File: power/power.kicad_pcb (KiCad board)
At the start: 2 copper layers, 100 x 100 mm, 25 parts, among them K1 RELAY_SPST, K2 RELAY_SPST, K3 RELAY_SPST, P1 CONTROL, P2 MAINS_INLET, P3 LOAD_OUTLET, Q1 BC817-40, Q2 BC817-40, Q3 BC817-40, U1 VTX214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

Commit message: Power: onboard fuses, better attempt at first pcb
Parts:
- added U4: TIC206M, Transistors_TO-220:TO-220_Neutral123_Vertical_LargePads, F.Cu at (122.0, 70.0)
- F1: footprint power:fuseholder -> power:5x20_clip
- F2: footprint power:fuseholder -> power:BS1362_clip
- K1: value RELAY_SPST -> MASTER_LIVE
- K2: value RELAY_SPST -> MASTER_NEUTRAL
- K3: value RELAY_SPST -> PREHEAT
- moved C4 216.9 mm to (124.0, 63.0), turned to 180 degrees
- moved R2 195.1 mm to (96.9, 230.8)
- moved R6 195.1 mm to (101.4, 230.8)
- moved C1 176.2 mm to (48.2, 238.5)
- moved C3 176.2 mm to (67.0, 236.8)
- moved Q1 176.2 mm to (86.7, 255.6)
- moved Q2 176.2 mm to (47.3, 232.0)
- moved R1 176.2 mm to (66.7, 230.4)
- moved R3 176.2 mm to (71.2, 230.4)
- moved U5 176.2 mm to (59.6, 235.0)
- moved Q3 176.2 mm to (86.7, 263.7)
- moved R4 172.7 mm to (122.0, 88.0), turned to 270 degrees
- moved C2 165.1 mm to (61.0, 216.0)
- moved P1 164.6 mm to (115.0, 273.0)
- moved R5 134.7 mm to (118.0, 63.0), turned to 180 degrees
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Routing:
- net MAINS_NEUTRAL: track 0.00 -> 81.8 mm
- net /EARTH: track 0.00 -> 70.1 mm
- net TRIAC_MAINS: track 0.00 -> 69.1 mm
- net SENSE_NEUTRAL: track 0.00 -> 50.4 mm
- net LOAD_LIVE: track 0.00 -> 47.7 mm
- net MAINS_LIVE: track 0.00 -> 40.9 mm
- net LOAD_NEUTRAL: track 0.00 -> 32.4 mm
- net Net-(U3-Pad4): track 0.00 -> 23.7 mm
- net Net-(F1-Pad2): track 0.00 -> 23.0 mm
- net Net-(F2-Pad1): track 0.00 -> 19.5 mm
- net Net-(R4-Pad2): track 0.00 -> 3.43 mm
- net Net-(C4-Pad2): track 0.00 -> 3.00 mm

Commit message: Removed neutral switching, more pcb mains rev
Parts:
- removed the K2 at (114.0, 98.0)
- removed the Q2 at (47.3, 232.0)
- removed the R2 at (96.9, 230.8)
- moved K1 13.5 mm to (94.5, 85.5)
- moved K2 10.6 mm to (110.0, 85.5)
- moved R3 8.08 mm to (119.0, 80.5)
- moved U3 7.83 mm to (121.5, 89.0)
- moved U2 6.04 mm to (71.5, 92.5)
- moved C4 5.70 mm to (120.5, 67.5), turned to 90 degrees
- moved F1 5.52 mm to (45.5, 63.5)
- moved F2 4.61 mm to (74.5, 52.0)
- moved U4 3.64 mm to (125.5, 69.0), turned to 270 degrees
- moved R4 3.04 mm to (121.0, 62.5), turned to 90 degrees
- renumbered K3 to K2, Q3 to Q2, R3 to R2, R4 to R3, R5 to R4, R6 to R5
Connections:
- U2 pad 1: SENSE_NEUTRAL -> LOAD_NEUTRAL
- U2 pad 2: SENSE_NEUTRAL -> LOAD_NEUTRAL
- U2 pad 3: SENSE_NEUTRAL -> LOAD_NEUTRAL
- U2 pad 4: SENSE_NEUTRAL -> LOAD_NEUTRAL
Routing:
- net SENSE_NEUTRAL: track 50.4 -> 0.00 mm
- net LOAD_NEUTRAL: track 32.4 -> 69.4 mm
- net MAINS_LIVE: track 40.9 -> 52.2 mm
- net MAINS_NEUTRAL: track 81.8 -> 93.0 mm
- net TRIAC_MAINS: track 69.1 -> 58.5 mm
- net Net-(U3-Pad4): track 23.7 -> 14.3 mm
- net Net-(F1-Pad2): track 23.0 -> 28.4 mm
- net LOAD_LIVE: track 47.7 -> 51.5 mm
- net Net-(F2-Pad1): track 19.5 -> 21.7 mm
- net Net-(C4-Pad2): track 3.00 -> 2.21 mm

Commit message: Power: Thermal switch based cutoff
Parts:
- U5: value DS18B20 -> 70°C; footprint power:to92-straight -> Wire_Connections_Bridges:WireConnection_1mmDrill
- moved U5 169.7 mm to (121.5, 77.0), turned to 90 degrees
- moved P1 109.0 mm to (117.5, 164.0), turned to 180 degrees
- moved Q1 95.6 mm to (91.2, 160.1)
- moved Q2 95.6 mm to (91.2, 168.2)
- moved C1 73.2 mm to (53.2, 165.5)
- moved C2 73.2 mm to (66.0, 143.0)
- moved C3 73.2 mm to (72.0, 163.8)
- moved R1 73.2 mm to (71.7, 157.4)
- moved R2 73.2 mm to (76.2, 157.4)
- moved R5 73.2 mm to (106.4, 157.8)
- moved F1 3.04 mm to (46.0, 66.5)
- moved R3 1.80 mm to (117.5, 81.5)
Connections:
- P1 pad 3: TEMP_SENSE -> Net-(P1-Pad3)
- R3 pad 1: TRIAC_MAINS -> Net-(R3-Pad1)
- U5 pad 1: GND -> Net-(R3-Pad1)
- U5 pad 2: TEMP_SENSE -> TRIAC_MAINS
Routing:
- net TRIAC_MAINS: track 58.5 -> 53.7 mm
- net Net-(R3-Pad1): track 0.00 -> 4.23 mm
- net MAINS_NEUTRAL: track 93.0 -> 94.9 mm
- net Net-(F1-Pad2): track 28.4 -> 26.7 mm
- net MAINS_LIVE: track 52.2 -> 50.5 mm

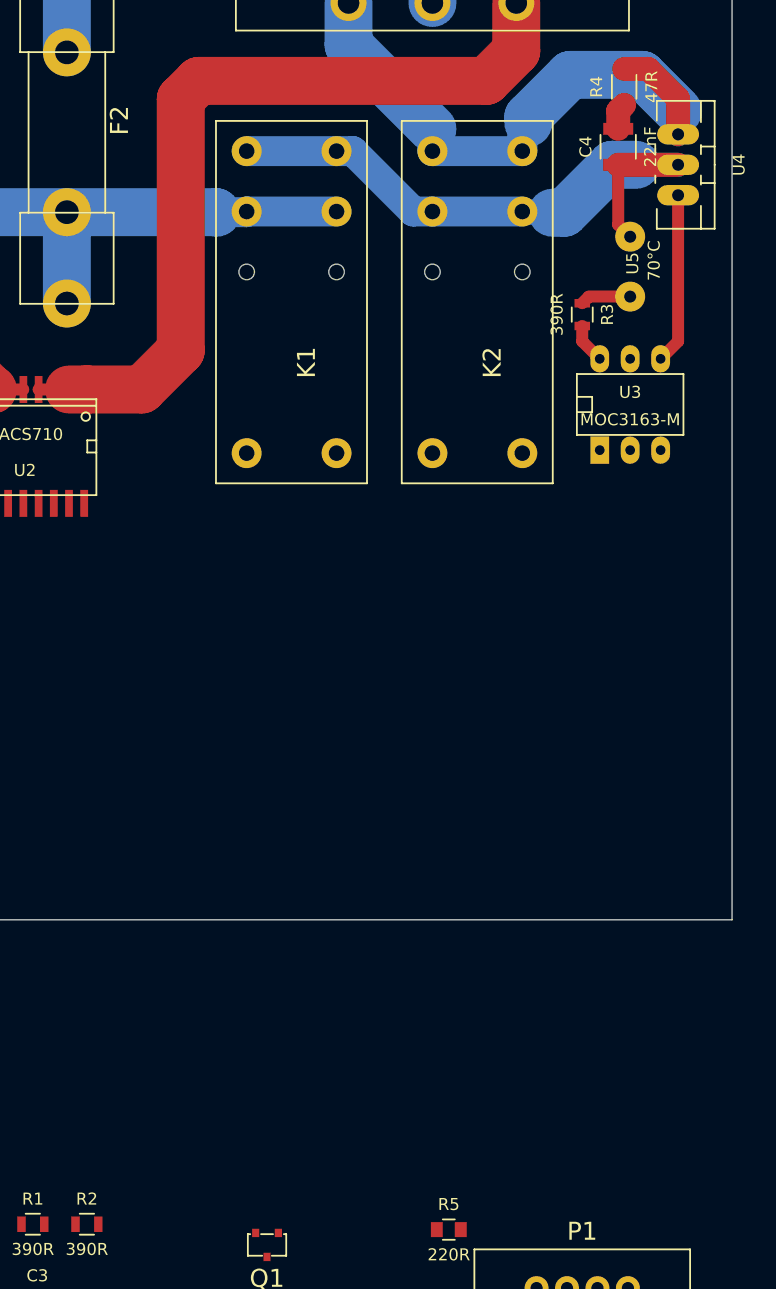
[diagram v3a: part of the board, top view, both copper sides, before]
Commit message: Updated TRIAC part, added LEDs.
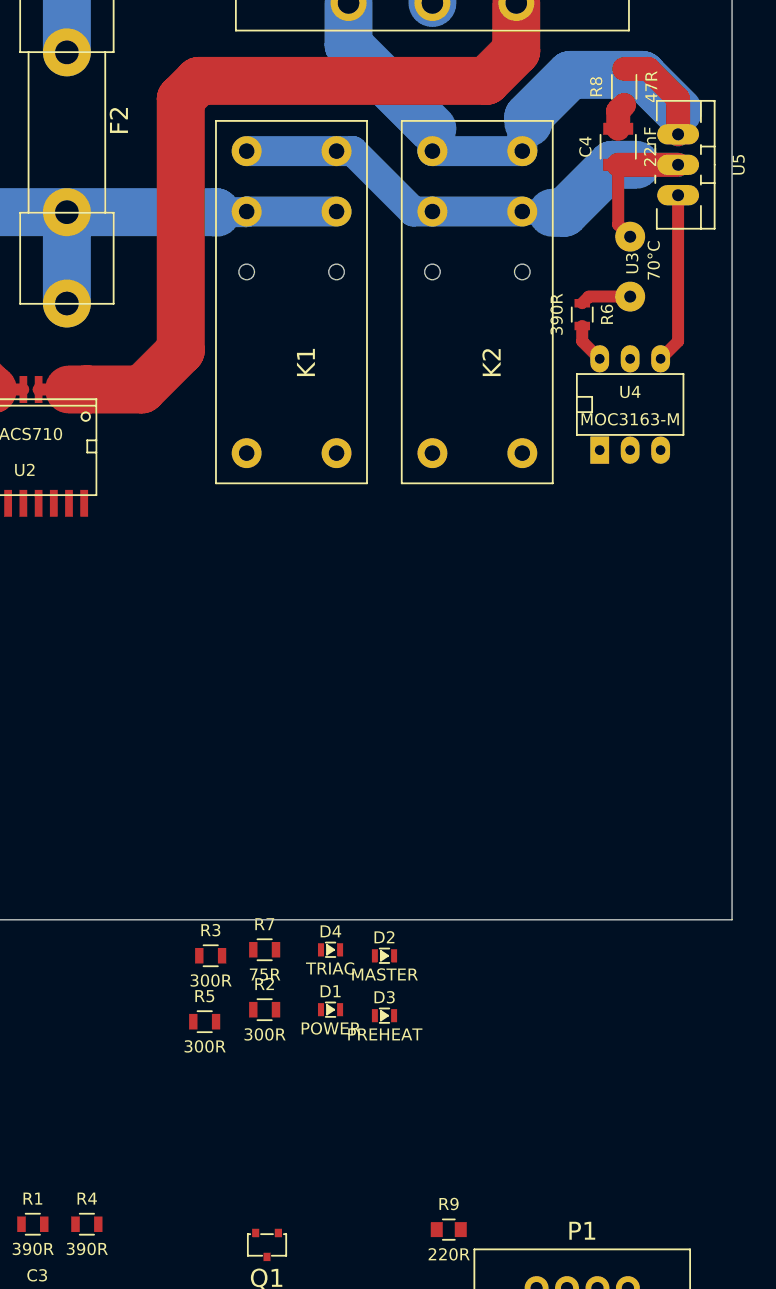
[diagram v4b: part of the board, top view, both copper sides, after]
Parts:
- added D1: POWER, power:LED-0805, F.Cu at (96.5, 139.5)
- added D2: MASTER, power:LED-0805, F.Cu at (101.0, 135.0)
- added D3: PREHEAT, power:LED-0805, F.Cu at (101.0, 140.0)
- added D4: TRIAC, power:LED-0805, F.Cu at (96.5, 134.5)
- added R2: 300R, Resistors_SMD:R_0805, F.Cu at (91.0, 139.5)
- added R3: 300R, Resistors_SMD:R_0805, F.Cu at (86.5, 135.0)
- added R5: 300R, Resistors_SMD:R_0805, F.Cu at (86.0, 140.5)
- added R7: 75R, Resistors_SMD:R_0805, F.Cu at (91.0, 134.5)
- U5: renamed from U4; value TIC206M -> BTA16-800BRG
- renumbered R2 to R4, R3 to R6, R4 to R8, R5 to R9, U5 to U3, U3 to U4

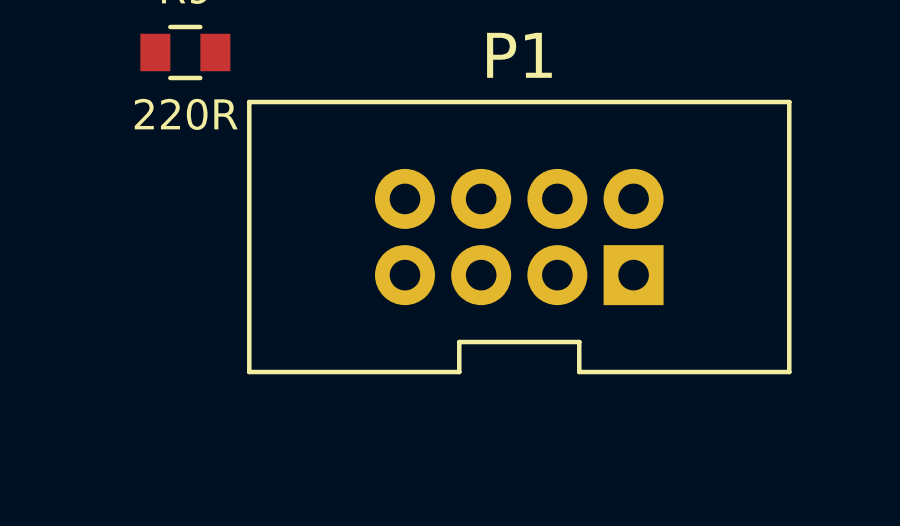
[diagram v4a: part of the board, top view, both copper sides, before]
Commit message: P: Updated connector footprint and pinout
Also decided to stick with ACS712 instead of cheaper/smaller ACS710 because the
former is SOICW instead of SOIC so has a bit more isolation distance.
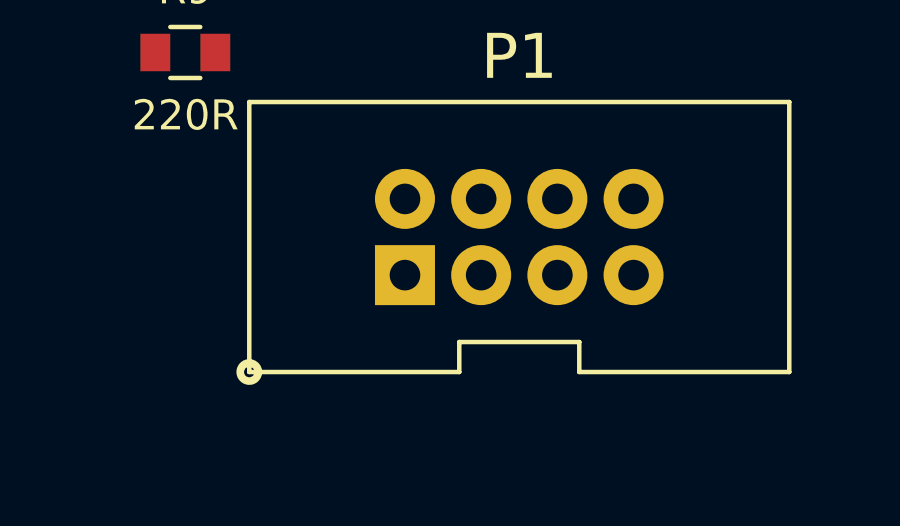
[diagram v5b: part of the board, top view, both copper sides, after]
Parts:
- P1: footprint power:TS821X08XXS100 -> control:2x4_100
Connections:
- P1 pad 3: Net-(P1-Pad3) -> I_SENSE
- P1 pad 5: I_SENSE -> Net-(P1-Pad5)
- P1 pad 7: +5V -> Net-(P1-Pad7)
- P1 pad 8: Net-(P1-Pad8) -> +5V

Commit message: Ppcb: first full route attempt
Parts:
- moved Q2 71.0 mm to (112.5, 100.5)
- moved C1 64.9 mm to (66.5, 102.0), turned to 180 degrees
- moved C3 62.9 mm to (75.0, 101.0)
- moved Q1 59.8 mm to (96.0, 100.5)
- moved D1 59.4 mm to (45.5, 109.0)
- moved R4 58.1 mm to (105.0, 107.0), turned to 180 degrees
- moved R9 57.9 mm to (119.5, 101.5), turned to 180 degrees
- moved R1 53.5 mm to (89.5, 107.0), turned to 180 degrees
- moved P1 52.8 mm to (89.0, 119.5), turned to 0 degrees
- moved R3 50.2 mm to (45.5, 106.0), turned to 180 degrees
- moved R7 46.4 mm to (119.0, 97.5), turned to 270 degrees
- moved R5 45.2 mm to (105.0, 99.5)
- moved R2 40.5 mm to (89.5, 99.0)
- moved C2 38.0 mm to (66.5, 105.0), turned to 180 degrees
- moved D4 37.8 mm to (119.5, 104.5)
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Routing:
- net +5V: track 0.00 -> 184.5 mm
- net TRIAC_TRIG: track 0.00 -> 61.0 mm, vias 0 -> 1
- net GND: track 0.00 -> 37.3 mm, vias 0 -> 5
- net I_SENSE: track 0.00 -> 32.1 mm
- net PREHEAT_RELAY: track 0.00 -> 28.0 mm, vias 0 -> 1
- net MASTER_RELAY: track 0.00 -> 18.7 mm, vias 0 -> 1
- net Net-(K2-Pad2): track 0.00 -> 15.2 mm
- net Net-(K1-Pad2): track 0.00 -> 13.1 mm
- net Net-(Q2-Pad1): track 0.00 -> 11.8 mm
- net Net-(Q1-Pad1): track 0.00 -> 11.0 mm
- net Net-(C2-Pad1): track 0.00 -> 9.20 mm
- net Net-(R9-Pad1): track 0.00 -> 9.10 mm
- net Net-(D4-Pad1): track 0.00 -> 8.55 mm
- net V_OFFSET: track 0.00 -> 5.09 mm
- net Net-(D2-Pad1): track 0.00 -> 4.06 mm
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- added copper zone on B.Cu, net GND

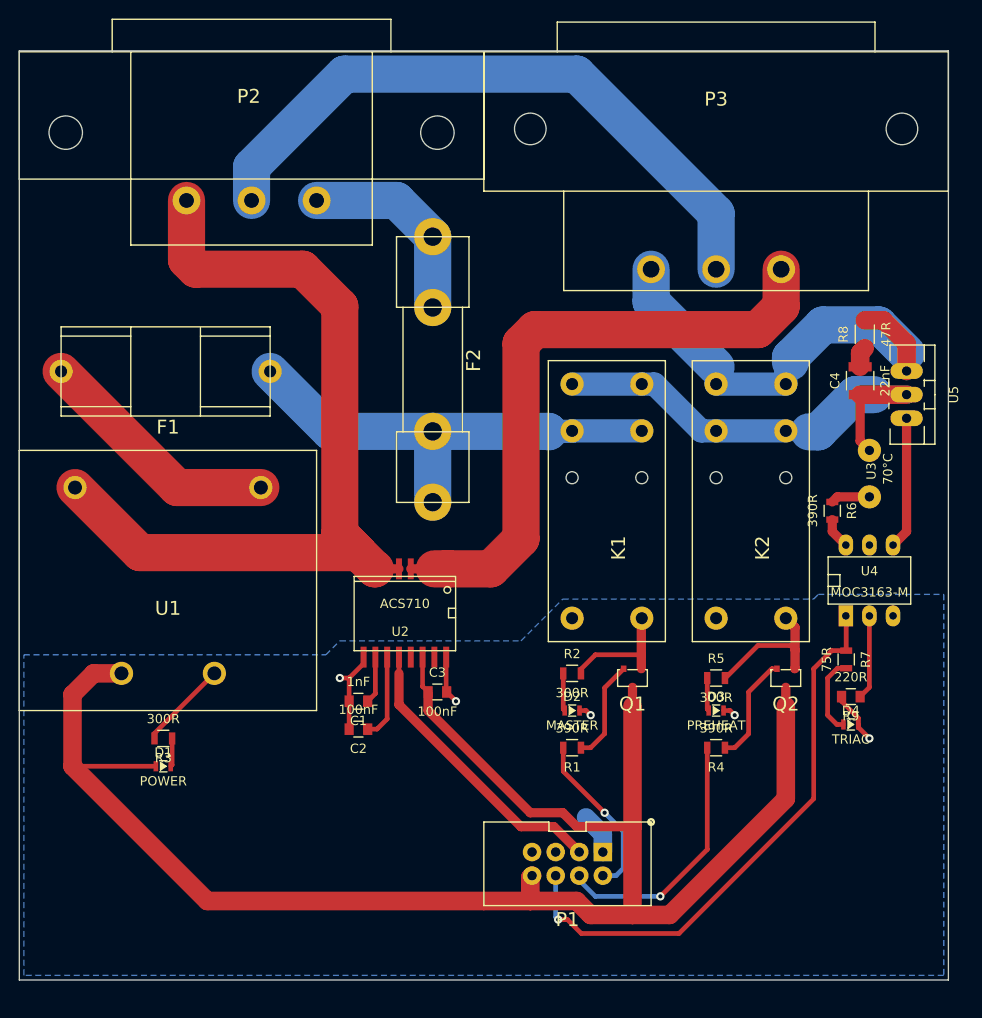
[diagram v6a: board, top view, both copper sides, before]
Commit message: Ppcb: triac heatsink and reroutes
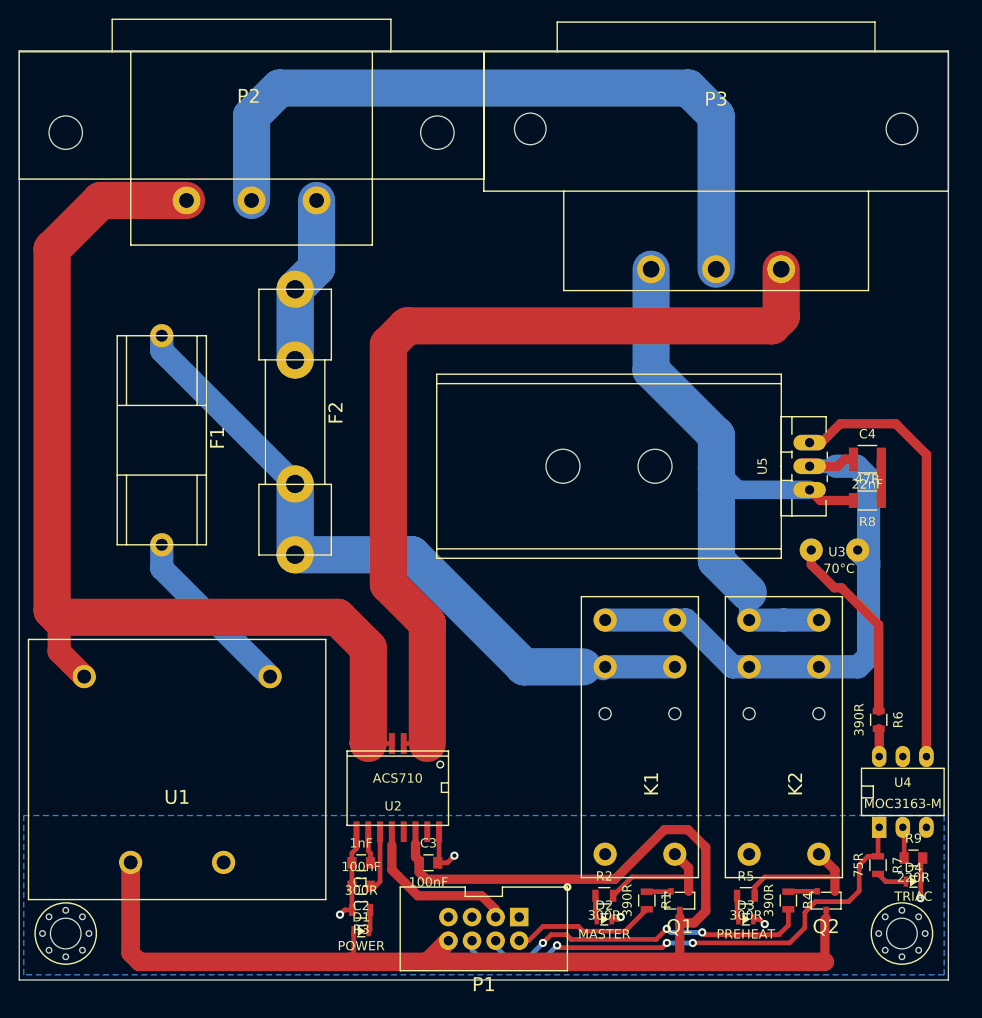
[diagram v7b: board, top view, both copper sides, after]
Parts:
- added M3_MOUNT: VAL**, control:M3_MOUNT, F.Cu at (125.0, 127.0)
- added M3_MOUNT: VAL**, control:M3_MOUNT, F.Cu at (35.0, 127.0)
- added REF**: TO220_hs, power:TO220_hs, F.Cu at (93.5, 76.7)
- moved R3 28.2 mm to (66.8, 124.5)
- moved D1 27.7 mm to (66.8, 126.7)
- moved K1 25.6 mm to (98.1, 110.9)
- moved K2 25.6 mm to (113.6, 110.9)
- moved Q1 24.5 mm to (101.1, 124.5)
- moved Q2 24.3 mm to (116.8, 124.5)
- moved R2 24.2 mm to (93.0, 122.9)
- moved R5 23.7 mm to (108.2, 122.9)
- moved R6 23.0 mm to (122.5, 104.0)
- moved U4 23.0 mm to (125.1, 111.8)
- moved D2 22.7 mm to (93.0, 125.5)
- moved D3 22.7 mm to (108.2, 125.5)
- moved R7 22.4 mm to (122.4, 119.6)
- moved U1 20.4 mm to (47.0, 109.3)
- moved U2 18.8 mm to (70.7, 111.3)
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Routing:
- net Net-(U4-Pad4): track 14.3 -> 47.3 mm
- net +5V: track 184.5 -> 153.0 mm
- net LOAD_NEUTRAL: track 69.4 -> 98.4 mm
- net MAINS_LIVE: track 50.5 -> 75.7 mm
- net MAINS_NEUTRAL: track 94.9 -> 113.4 mm
- net Net-(R6-Pad1): track 4.23 -> 20.8 mm
- net LOAD_LIVE: track 51.5 -> 65.9 mm
- net I_SENSE: track 32.1 -> 17.8 mm
- net GND: track 37.3 -> 23.4 mm
- net TRIAC_MAINS: track 53.7 -> 64.3 mm
- net PREHEAT_RELAY: track 28.0 -> 37.4 mm, vias 1 -> 3
- net Net-(Q2-Pad1): track 11.8 -> 3.13 mm
- net Net-(Q1-Pad1): track 11.0 -> 2.62 mm
- net /EARTH: track 70.0 -> 78.1 mm
- net Net-(F1-Pad2): track 26.7 -> 19.0 mm
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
